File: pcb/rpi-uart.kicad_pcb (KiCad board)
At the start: 2 copper layers, 21 x 39.4 mm, 28 parts, among them J1 Conn_01x05, J2 USB_OTG, J3 Conn_01x05, J4 GS2, J5 GS2, J6 5v, J7 3.3v, SW1 SW_Push_SPDT, U1 CH340g, U2 TLV1117-33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

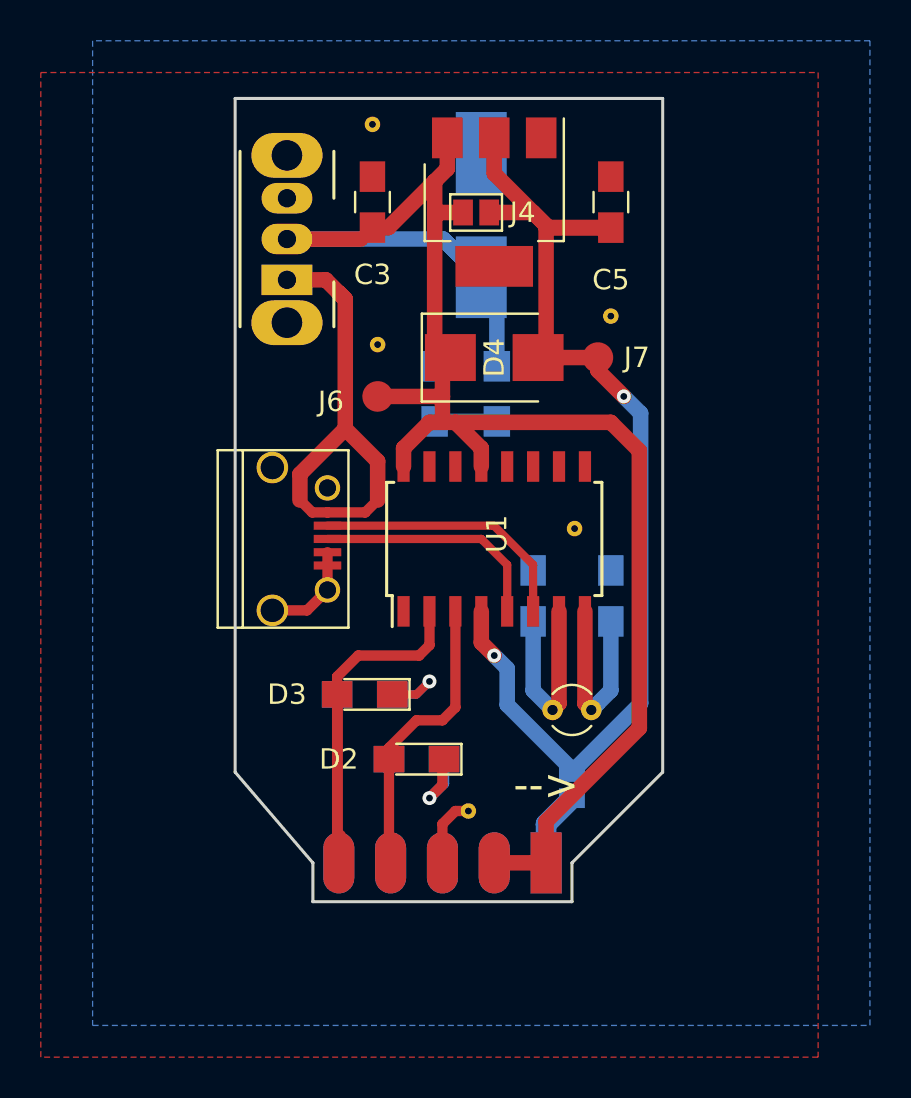
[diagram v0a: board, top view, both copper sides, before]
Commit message: v0.1.1: added missing silk, updated docs and images
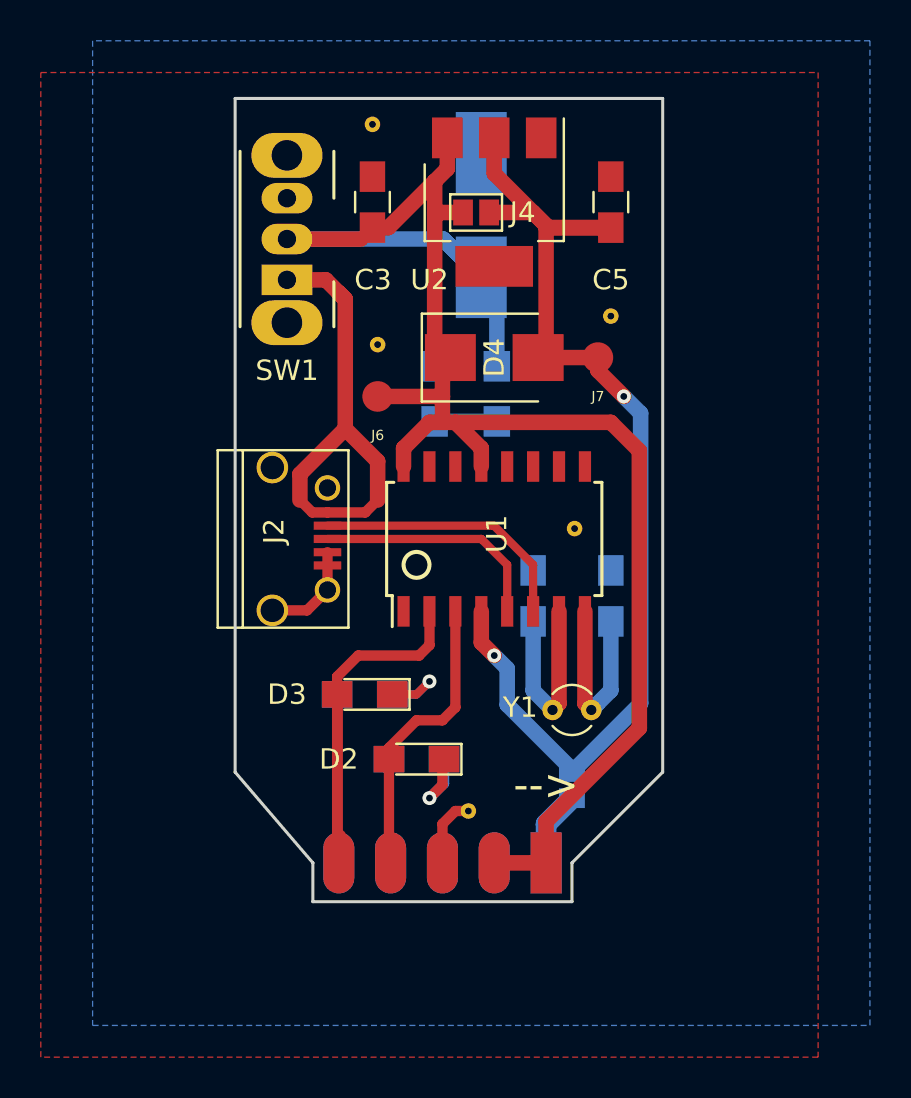
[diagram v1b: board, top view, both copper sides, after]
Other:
- board text added: "rpi-uart [v0.1.1]"
- board text removed: "rpi-uart [v0.1]"
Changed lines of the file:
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@@
     (area 133.909999 57.074999 155.015001 96.595001)
     (thickness 1.6)
-    (drawings 12)
+    (drawings 13)
     (tracks 148)
     (zones 0)
@@
     (pad_to_mask_clearance 0.2)
     (aux_axis_origin 0 0)
-    (visible_elements FFFEFF7F)
+    (visible_elements FFFEFFFF)
     (pcbplotparams
       (layerselection 0x010f0_80000001)
@@
     (descr "CuK miniature slide switch, OS series, SPDT, right angle, http://www.ckswitches.com/media/1428/os.pdf")
     (tags "switch SPDT")
-    (fp_text reference SW1 (at 1.4 -3.6 90) (layer F.SilkS) hide
+    (fp_text reference SW1 (at -4.445 0 180) (layer F.SilkS)
       (effects (font (size 1 1) (thickness 0.15)))
     )
@@
     (tags "CMS SOT")
     (attr smd)
-    (fp_text reference U2 (at 3.175 -3.81 540) (layer F.SilkS) hide
+    (fp_text reference U2 (at 3.81 3.175 360) (layer F.SilkS)
       (effects (font (size 1 1) (thickness 0.15)))
     )
@@
     (tags "USB USB_B USB_micro USB_OTG")
     (attr smd)
-    (fp_text reference J2 (at -0.381 1.27 270) (layer F.SilkS) hide
+    (fp_text reference J2 (at -0.381 1.27 270) (layer F.SilkS)
       (effects (font (size 1 1) (thickness 0.15)))
     )
@@
     (tags "capacitor 0805")
     (attr smd)
-    (fp_text reference C3 (at 3.556 0 540) (layer F.SilkS)
+    (fp_text reference C3 (at 3.81 -0.0254 540) (layer F.SilkS)
       (effects (font (size 1 1) (thickness 0.15)))
     )
@@
     (descr "Crystal THT C26-LF 6.5mm length 2.06mm diameter")
     (tags ['C26-LF'])
-    (fp_text reference Y1 (at 3.81 0 270) (layer F.SilkS) hide
+    (fp_text reference Y1 (at -1.5875 -0.127) (layer F.SilkS)
       (effects (font (size 1 1) (thickness 0.15)))
     )
@@
     (tags "Mesurement Point Round SMD Pad 1.5mm")
     (attr virtual)
-    (fp_text reference J6 (at -2.286 0.254) (layer F.SilkS)
-      (effects (font (size 1 1) (thickness 0.15)))
+    (fp_text reference J6 (at 0 1.905) (layer F.SilkS)
+      (effects (font (size 0.5 0.5) (thickness 0.125)))
     )
     (fp_text value 5v (at 0 2) (layer F.Fab)
@@
     (tags "Mesurement Point Round SMD Pad 1.5mm")
     (attr virtual)
-    (fp_text reference J7 (at 1.905 0) (layer F.SilkS)
-      (effects (font (size 1 1) (thickness 0.15)))
+    (fp_text reference J7 (at 0 1.905) (layer F.SilkS)
+      (effects (font (size 0.5 0.5) (thickness 0.125)))
     )
     (fp_text value 3.3v (at 0 2) (layer F.Fab)
@@
       (net 2 GND))
   )
-  (gr_text "rpi-uart\n[v0.1]" (at 143.51 78.74) (layer B.SilkS)
+  (gr_circle (center 142.875 80.01) (end 143.51 80.01) (layer F.SilkS) (width 0.2))
+  (gr_text "rpi-uart\n[v0.1.1]" (at 143.51 78.74) (layer B.SilkS)
     (effects (font (size 1.27 1.27) (thickness 0.1905)) (justify mirror))
   )
